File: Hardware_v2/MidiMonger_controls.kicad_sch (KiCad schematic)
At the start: 32 parts, among them J1 Conn_01x09_Male, J10 Gate5_Out, J11 Gate6_Out, J12 Gate7_Out, J13 Gate8_Out, J14 CV1_Out, J15 CV2_Out, J16 CV3_Out, J17 CV4_Out, J18 USB_C_Receptacle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

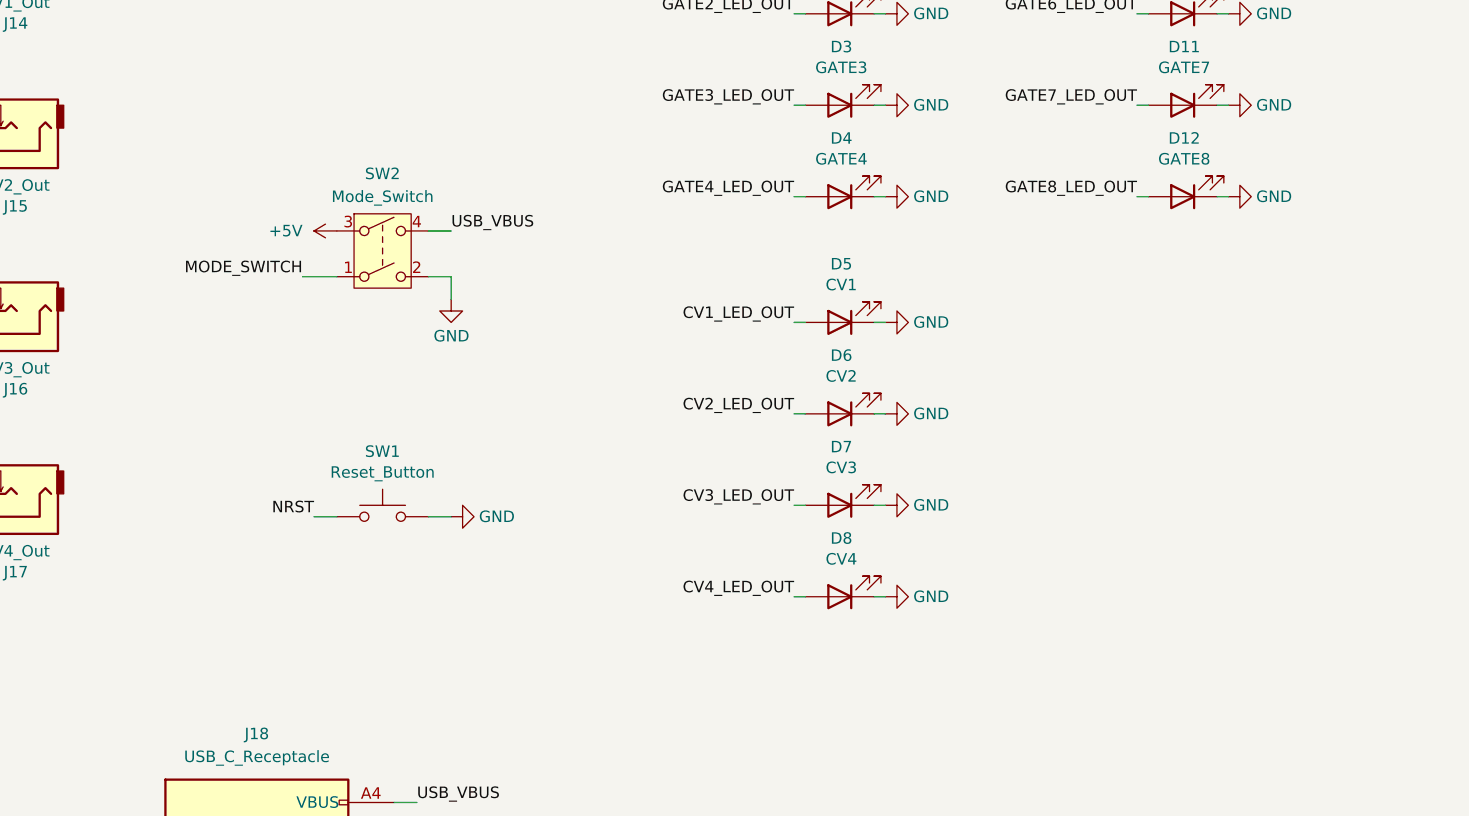
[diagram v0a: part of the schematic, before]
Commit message: Laying out panel
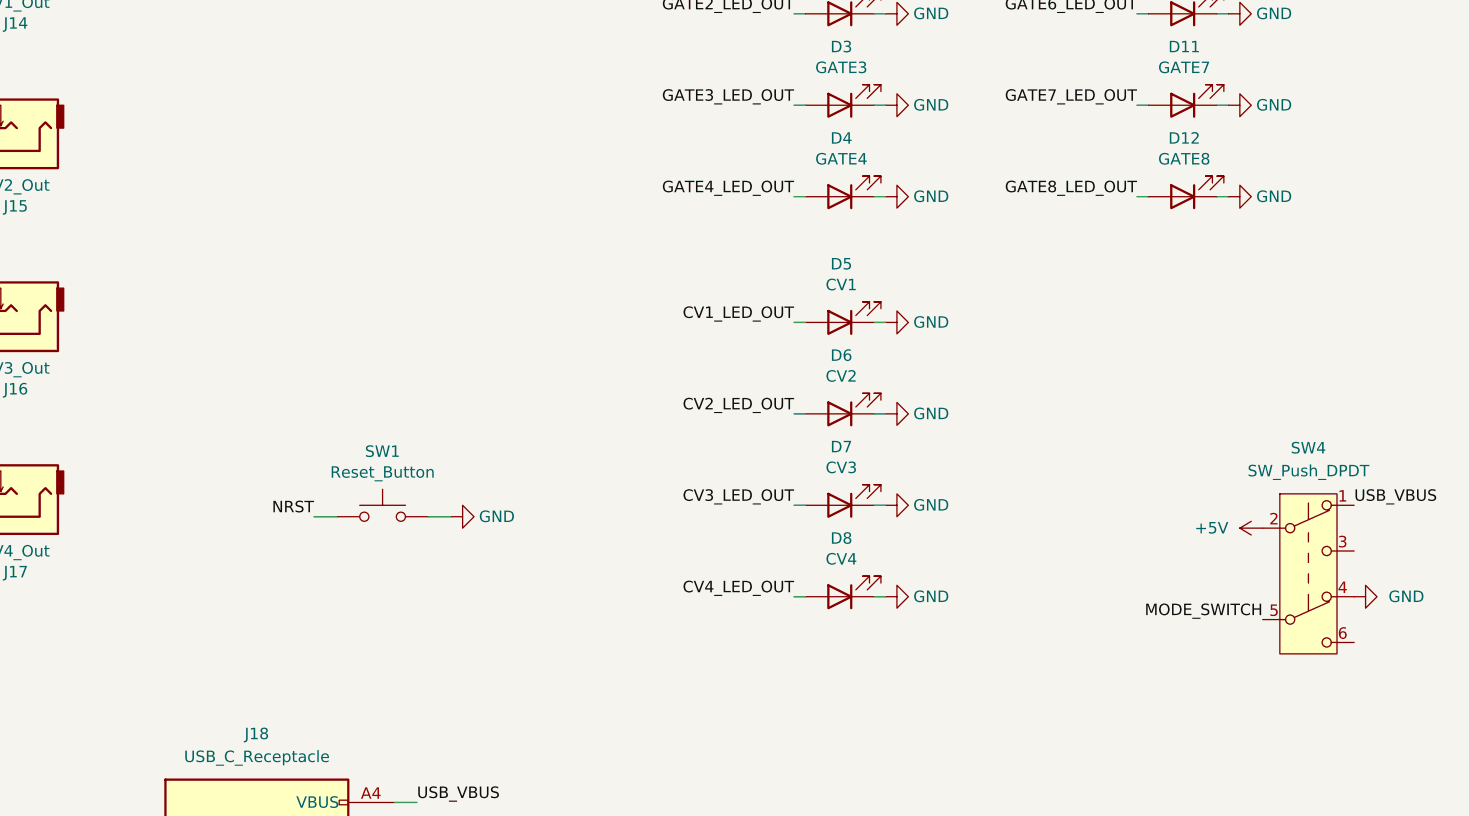
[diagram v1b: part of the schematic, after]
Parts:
- removed SW2: Mode_Switch, symbol Switch:SW_DPST
- added SW4: SW_Push_DPDT, Custom_Footprints:100DP6T1B1M2QE_ON_ON_ON, symbol Switch:SW_Push_DPDT
- D1, D10, D11, D12, D2, D3, D4, D5, D6, D7, D8, D9: footprint LED_THT:LED_D3.0mm_FlatTop -> Custom_Footprints:LED_D3.0mm
- SW1: footprint Buttons_Switches_THT:SW_PUSH_6mm -> Button_Switch_THT:SW_PUSH_6mm
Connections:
- net +5V: now also SW4.2 (B)
- net GND: now also SW4.4 (A)
- net MODE_SWITCH: now also SW4.5 (B)
- net USB_VBUS: now also SW4.1 (A)

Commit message: Gerbers prepared for manufacture
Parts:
- J1, J2: value Conn_01x09_Male -> Conn_01x09; footprint Connector_PinHeader_2.54mm:PinHeader_1x09_P2.54mm_Vertical -> Connector_PinSocket_2.54mm:PinSocket_1x09_P2.54mm_Vertical; symbol Connector:Conn_01x09_Pin -> Connector:Conn_01x09_Socket
- J3, J4: value Conn_01x08_Male -> Conn_01x10; footprint Connector_PinHeader_2.54mm:PinHeader_1x10_P2.54mm_Vertical -> Connector_PinSocket_2.54mm:PinSocket_1x10_P2.54mm_Vertical; symbol Connector:Conn_01x10_Pin -> Connector:Conn_01x10_Socket
- SW4: value SW_Push_DPDT -> Host_Device_Switch
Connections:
- no-connect marks 25 -> 29
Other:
- note added: "Connectors"
- note added: "LEDs"
- note added: "MIDI In"
- note added: "Outputs"
- note added: "Switches"
- note added: "USB"
- title: MIDI Monger -> MIDI Monger Controls
- moved on the sheet: D1, D10, D11, D12, D2, D3, D4, D5, D6, D7, D8, D9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
